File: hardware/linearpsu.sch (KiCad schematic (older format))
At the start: 3 parts

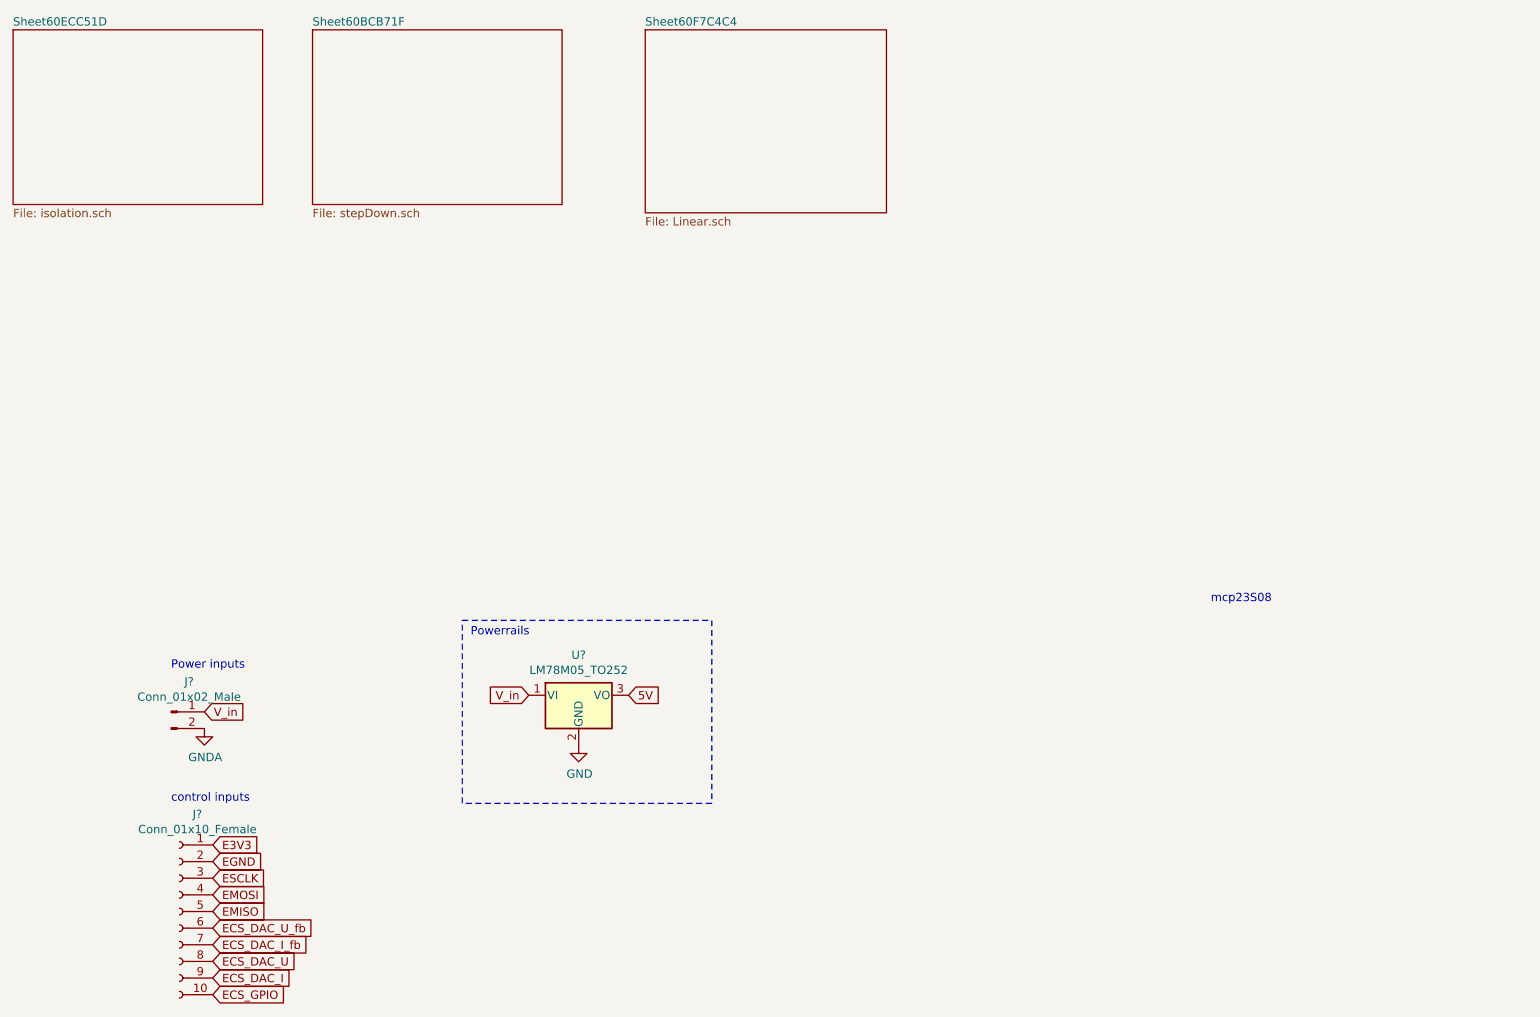
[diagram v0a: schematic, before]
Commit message: switched to xl4016 and worked on control board
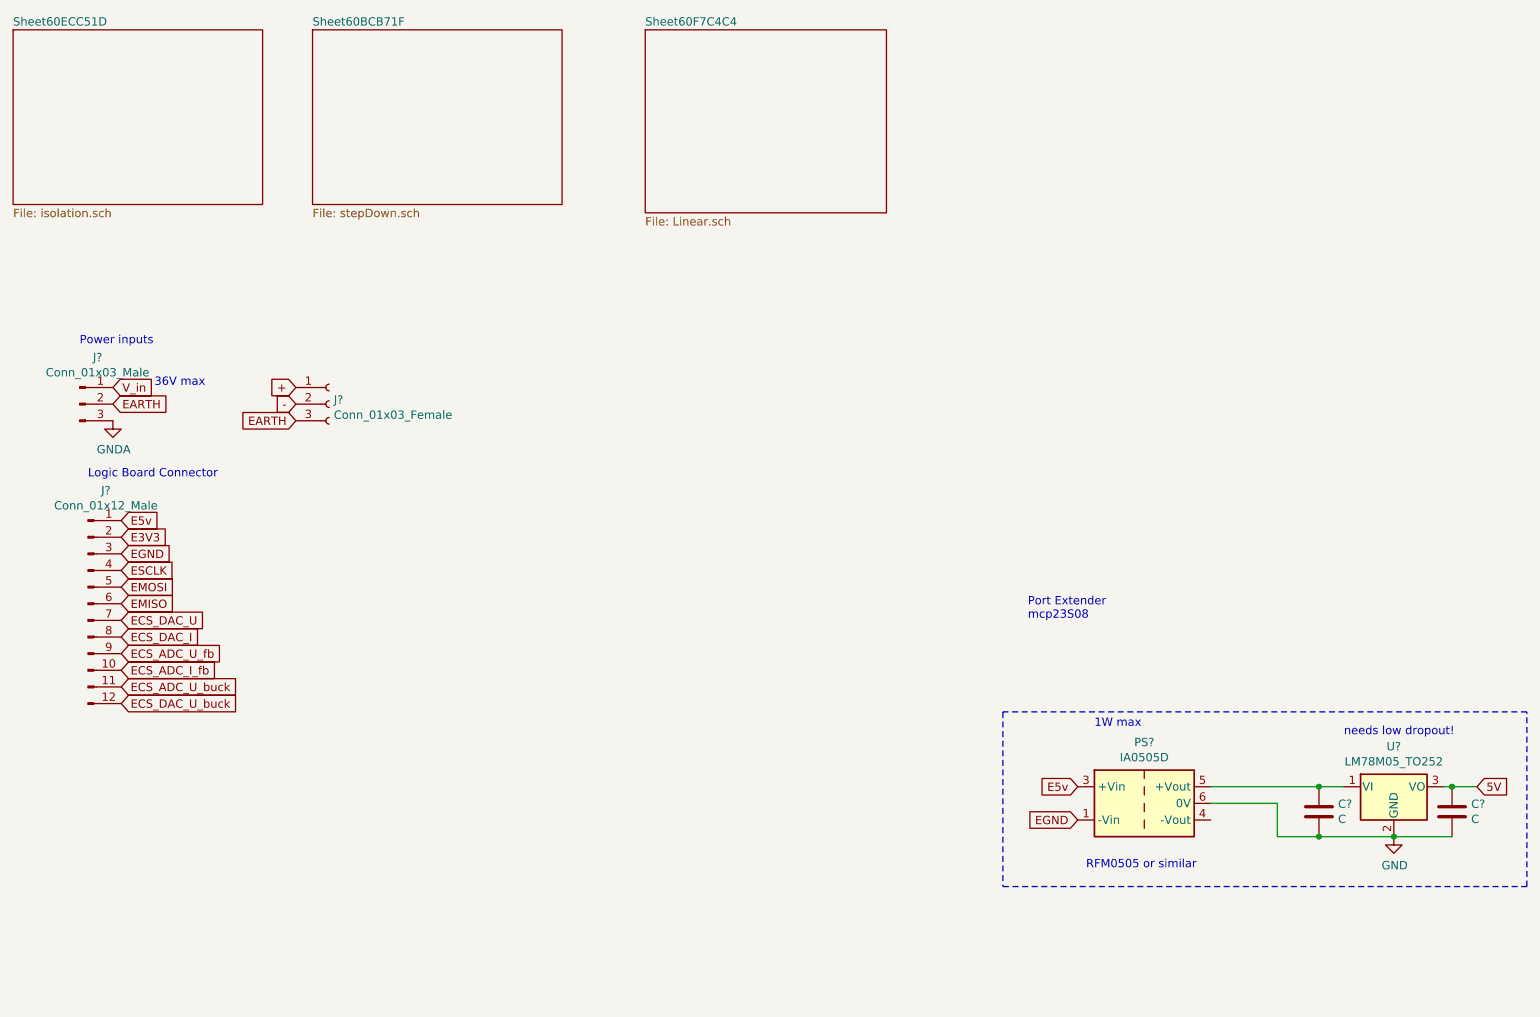
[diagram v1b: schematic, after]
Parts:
- removed J?: Conn_01x10_Female, symbol Connector:Conn_01x10_Female
- removed J?: Conn_01x02_Male, symbol Connector:Conn_01x02_Male
- added C? (x2): C, symbol Device:C
- added J?: Conn_01x12_Male, symbol Connector:Conn_01x12_Male
- added J?: Conn_01x03_Female, symbol Connector:Conn_01x03_Female
- added J?: Conn_01x03_Male, symbol Connector:Conn_01x03_Male
- added PS?: IA0505D, Converter_DCDC:Converter_DCDC_XP_POWER-IAxxxxD_THT, symbol Converter_DCDC:IA0505D
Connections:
- net 5V: now also C?.1
- net E3V3: now also J?.2 (Pin_2)
- net ECS_DAC_I: now also J?.8 (Pin_8)
- net ECS_DAC_U: now also J?.7 (Pin_7)
- net EGND: now also J?.3 (Pin_3), PS?.1 (-Vin)
- net EMISO: now also J?.6 (Pin_6)
- net EMOSI: now also J?.5 (Pin_5)
- net ESCLK: now also J?.4 (Pin_4)
- net GND: now also C?.2, C?.2, PS?.6 (0V)
- net GNDA: now also J?.3 (Pin_3)
- net V_in: now also J?.1 (Pin_1); no longer U?.1 (VI)
- new net: C?.1, PS?.5 (+Vout), U?.1 (VI)
- new net +: J?.1 (Pin_1)
- new net -: J?.2 (Pin_2)
- new net E5v: J?.1 (Pin_1), PS?.3 (+Vin)
- new net EARTH: J?.2 (Pin_2), J?.3 (Pin_3)
- new net ECS_ADC_I_fb: J?.10 (Pin_10)
- new net ECS_ADC_U_buck: J?.11 (Pin_11)
- new net ECS_ADC_U_fb: J?.9 (Pin_9)
- new net ECS_DAC_U_buck: J?.12 (Pin_12)
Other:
- note added: "1W max"
- note added: "36V max"
- note added: "Logic Board Connector"
- note added: "Port Extender\nmcp23S08"
- note added: "RFM0505 or similar"
- note added: "needs low dropout!"
- note removed: "Powerrails"
- note removed: "control inputs"
- note removed: "mcp23S08"
- moved on the sheet: U?
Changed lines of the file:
@@
 Comment4 ""
 $EndDescr
-Text GLabel 2100 4950 2    50   Input ~ 0
+Text GLabel 1550 3000 2    50   Input ~ 0
 V_in
 $Comp
 L power:GNDA #PWR0102
 U 1 1 6016DF96
-P 2100 5050
-F 0 "#PWR0102" H 2100 4800 50  0001 C CNN
-F 1 "GNDA" H 2105 4877 50  0000 C CNN
-F 2 "" H 2100 5050 50  0001 C CNN
-F 3 "" H 2100 5050 50  0001 C CNN
-	1    2100 5050
-	1    0    0    -1
-$EndComp
-Text Notes 1900 4700 0    50   ~ 0
+P 1550 3200
+F 0 "#PWR0102" H 1550 2950 50  0001 C CNN
+F 1 "GNDA" H 1555 3027 50  0000 C CNN
+F 2 "" H 1550 3200 50  0001 C CNN
+F 3 "" H 1550 3200 50  0001 C CNN
+	1    1550 3200
+	1    0    0    -1
+$EndComp
+Text Notes 1350 2750 0    50   ~ 0
 Power inputs
 $Comp
 L Regulator_Linear:LM78M05_TO252 U?
 U 1 1 6095F810
-P 4350 4850
-F 0 "U?" H 4350 5092 50  0000 C CNN
-F 1 "LM78M05_TO252" H 4350 5001 50  0000 C CNN
-F 2 "Package_TO_SOT_SMD:TO-252-2" H 4350 5075 50  0001 C CIN
-F 3 "https://www.onsemi.com/pub/Collateral/MC78M00-D.PDF" H 4350 4800 50  0001 C CNN
-	1    4350 4850
-	1    0    0    -1
-$EndComp
-Text GLabel 4650 4850 2    50   Input ~ 0
+P 9250 5400
+F 0 "U?" H 9250 5642 50  0000 C CNN
+F 1 "LM78M05_TO252" H 9250 5551 50  0000 C CNN
+F 2 "Package_TO_SOT_SMD:TO-252-2" H 9250 5625 50  0001 C CIN
+F 3 "https://www.onsemi.com/pub/Collateral/MC78M00-D.PDF" H 9250 5350 50  0001 C CNN
+	1    9250 5400
+	1    0    0    -1
+$EndComp
+Text GLabel 9750 5400 2    50   Input ~ 0
 5V
 $Comp
 L power:GND #PWR?
 U 1 1 60961853
-P 4350 5150
-F 0 "#PWR?" H 4350 4900 50  0001 C CNN
-F 1 "GND" H 4355 4977 50  0000 C CNN
-F 2 "" H 4350 5150 50  0001 C CNN
-F 3 "" H 4350 5150 50  0001 C CNN
-	1    4350 5150
-	1    0    0    -1
-$EndComp
-Text GLabel 4050 4850 0    50   Input ~ 0
-V_in
-Text GLabel 2150 5950 2    50   Input ~ 0
+P 9250 5700
+F 0 "#PWR?" H 9250 5450 50  0001 C CNN
+F 1 "GND" H 9255 5527 50  0000 C CNN
+F 2 "" H 9250 5700 50  0001 C CNN
+F 3 "" H 9250 5700 50  0001 C CNN
+	1    9250 5700
+	1    0    0    -1
+$EndComp
+Text GLabel 1600 4100 2    50   Input ~ 0
 ESCLK
-Text GLabel 2150 6050 2    50   Input ~ 0
+Text GLabel 1600 4200 2    50   Input ~ 0
 EMOSI
-Text GLabel 2150 6150 2    50   Input ~ 0
+Text GLabel 1600 4300 2    50   Input ~ 0
 EMISO
-$Comp
-L Connector:Conn_01x10_Female J?
-U 1 1 60C5AB16
-P 1950 6150
-F 0 "J?" H 1842 6735 50  0000 C CNN
-F 1 "Conn_01x10_Female" H 1842 6644 50  0000 C CNN
-F 2 "" H 1950 6150 50  0001 C CNN
-F 3 "~" H 1950 6150 50  0001 C CNN
-	1    1950 6150
-	-1   0    0    -1
-$EndComp
-Text GLabel 2150 5750 2    50   Input ~ 0
+Text GLabel 1600 3900 2    50   Input ~ 0
 E3V3
-Text GLabel 2150 5850 2    50   Input ~ 0
+Text GLabel 1600 4000 2    50   Input ~ 0
 EGND
 $Sheet
@@
 F1 "Linear.sch" 50
 $EndSheet
-Wire Notes Line
-	3650 5500 3650 4400
-Wire Notes Line
-	3650 4400 5150 4400
-Text Notes 3700 4500 0    50   ~ 0
-Powerrails
-Wire Notes Line
-	5150 5500 3650 5500
-Wire Notes Line
-	5150 4400 5150 5500
-Text GLabel 2150 6250 2    50   Input ~ 0
-ECS_DAC_U_fb
-Text GLabel 2150 6350 2    50   Input ~ 0
-ECS_DAC_I_fb
-Text GLabel 2150 6450 2    50   Input ~ 0
+Text GLabel 1600 4400 2    50   Input ~ 0
 ECS_DAC_U
-Text GLabel 2150 6550 2    50   Input ~ 0
+Text GLabel 1600 4500 2    50   Input ~ 0
 ECS_DAC_I
-Text GLabel 2150 6650 2    50   Input ~ 0
-ECS_GPIO
-$Comp
-L Connector:Conn_01x02_Male J?
-U 1 1 61122DA7
-P 1900 4950
-F 0 "J?" H 2008 5131 50  0000 C CNN
-F 1 "Conn_01x02_Male" H 2008 5040 50  0000 C CNN
-F 2 "" H 1900 4950 50  0001 C CNN
-F 3 "~" H 1900 4950 50  0001 C CNN
-	1    1900 4950
-	1    0    0    -1
-$EndComp
-Text Notes 1900 5500 0    50   ~ 0
-control inputs
-Text Notes 8150 4300 0    50   ~ 0
-mcp23S08
+Text GLabel 1600 4600 2    50   Input ~ 0
+ECS_ADC_U_fb
+Text GLabel 1600 4700 2    50   Input ~ 0
+ECS_ADC_I_fb
+Text Notes 1400 3550 0    50   ~ 0
+Logic Board Connector
+Text Notes 7050 4400 0    50   ~ 0
+Port Extender\nmcp23S08
 $Sheet
 S 2750 850  1500 1050
@@
 F1 "stepDown.sch" 50
 $EndSheet
+Text Notes 1800 3000 0    50   ~ 0
+36V max
+$Comp
+L Converter_DCDC:IA0505D PS?
+U 1 1 60F0F219
+P 7750 5500
+F 0 "PS?" H 7750 5867 50  0000 C CNN
+F 1 "IA0505D" H 7750 5776 50  0000 C CNN
+F 2 "Converter_DCDC:Converter_DCDC_XP_POWER-IAxxxxD_THT" H 6700 5250 50  0001 L CNN
+F 3 "https://www.xppower.com/pdfs/SF_IA.pdf" H 8800 5200 50  0001 L CNN
+	1    7750 5500
+	1    0    0    -1
+$EndComp
+Text GLabel 1600 3800 2    50   Input ~ 0
+E5v
+Text GLabel 7350 5400 0    50   Input ~ 0
+E5v
+Text GLabel 7350 5600 0    50   Input ~ 0
+EGND
+Wire Wire Line
+	8150 5500 8550 5500
+Wire Wire Line
+	8550 5500 8550 5700
+Connection ~ 9250 5700
+$Comp
+L Device:C C?
+U 1 1 60F30304
+P 8800 5550
+F 0 "C?" H 8915 5596 50  0000 L CNN
+F 1 "C" H 8915 5505 50  0000 L CNN
+F 2 "" H 8838 5400 50  0001 C CNN
+F 3 "~" H 8800 5550 50  0001 C CNN
+	1    8800 5550
+	1    0    0    -1
+$EndComp
+Wire Wire Line
+	8950 5400 8800 5400
+Wire Wire Line
+	8800 5700 9250 5700
+Wire Wire Line
+	8800 5700 8550 5700
+Connection ~ 8800 5700
+Wire Wire Line
+	8150 5400 8800 5400
+Connection ~ 8800 5400
+$Comp
+L Device:C C?
+U 1 1 60F34BE5
+P 9600 5550
+F 0 "C?" H 9715 5596 50  0000 L CNN
+F 1 "C" H 9715 5505 50  0000 L CNN
+F 2 "" H 9638 5400 50  0001 C CNN
+F 3 "~" H 9600 5550 50  0001 C CNN
+	1    9600 5550
+	1    0    0    -1
+$EndComp
+Wire Wire Line
+	9550 5400 9600 5400
+Connection ~ 9600 5400
+Wire Wire Line
+	9600 5400 9750 5400
+Wire Wire Line
+	9600 5700 9250 5700
+Text GLabel 1600 4800 2    50   Input ~ 0
+ECS_ADC_U_buck
+Text GLabel 1600 4900 2    50   Input ~ 0
+ECS_DAC_U_buck
+$Comp
+L Connector:Conn_01x12_Male J?
+U 1 1 60F69F34
+P 1400 4300
+F 0 "J?" H 1508 4981 50  0000 C CNN
+F 1 "Conn_01x12_Male" H 1508 4890 50  0000 C CNN
+F 2 "" H 1400 4300 50  0001 C CNN
+F 3 "~" H 1400 4300 50  0001 C CNN
+	1    1400 4300
+	1    0    0    -1
+$EndComp
+Text Notes 8950 5100 0    50   ~ 0
+needs low dropout!
+Wire Notes Line
+	6900 6000 10050 6000
+Wire Notes Line
+	10050 6000 10050 4950
+Wire Notes Line
+	10050 4950 6900 4950
+Wire Notes Line
+	6900 4950 6900 6000
+Text Notes 7400 5900 0    50   ~ 0
+RFM0505 or similar
+Text Notes 7450 5050 0    50   ~ 0
+1W max
+Text GLabel 2650 3000 0    50   Input ~ 0
++
+Text GLabel 2650 3100 0    50   Input ~ 0
+-
+Text GLabel 2650 3200 0    50   Input ~ 0
+EARTH
+$Comp
+L Connector:Conn_01x03_Female J?
+U 1 1 610AB1BB
+P 2850 3100
+F 0 "J?" H 2878 3126 50  0000 L CNN
+F 1 "Conn_01x03_Female" H 2878 3035 50  0000 L CNN
+F 2 "" H 2850 3100 50  0001 C CNN
+F 3 "~" H 2850 3100 50  0001 C CNN
+	1    2850 3100
+	1    0    0    -1
+$EndComp
+$Comp
+L Connector:Conn_01x03_Male J?
+U 1 1 610B2348
+P 1350 3100
+F 0 "J?" H 1458 3381 50  0000 C CNN
+F 1 "Conn_01x03_Male" H 1458 3290 50  0000 C CNN
+F 2 "" H 1350 3100 50  0001 C CNN
+F 3 "~" H 1350 3100 50  0001 C CNN
+	1    1350 3100
+	1    0    0    -1
+$EndComp
+Text GLabel 1550 3100 2    50   Input ~ 0
+EARTH
 $EndSCHEMATC
